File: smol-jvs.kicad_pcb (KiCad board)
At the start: 2 copper layers, 68 x 55 mm, 15 parts, among them J1 USB_B, J2 Misc, J3 Dips, J5 Power, J6 Controls, Q1 AO3400A, U1 ISL3175EIBZ-T, U2 Pico

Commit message: new gerbers and minor updates
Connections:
- U2 pad 20: /dip3 -> unconnected-(U2-Pad20)
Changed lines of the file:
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@@
   (net 41 "unconnected-(H3-Pad1)")
   (net 42 "unconnected-(H4-Pad1)")
+  (net 43 "unconnected-(U2-Pad20)")
   (footprint "Resistor_SMD:R_0805_2012Metric" (layer "F.Cu")
     (at 190.8 66.65 180)
@@
       (net 33 "/b_service") (pinfunction "GPIO14") (pintype "bidirectional"))
     (pad "20" thru_hole oval locked (at -8.89 24.13) (size 1.7 1.7) (drill 1.02) (layers *.Cu *.Mask)
-      (net 37 "/dip3") (pinfunction "GPIO15") (pintype "bidirectional"))
+      (net 43 "unconnected-(U2-Pad20)") (pinfunction "GPIO15") (pintype "bidirectional+no_connect"))
     (pad "20" smd rect locked (at -8.89 24.13) (size 3.5 1.7) (drill (offset -0.9 0)) (layers "F.Cu" "F.Mask")
-      (net 37 "/dip3") (pinfunction "GPIO15") (pintype "bidirectional"))
+      (net 43 "unconnected-(U2-Pad20)") (pinfunction "GPIO15") (pintype "bidirectional+no_connect"))
     (pad "21" smd rect locked (at 8.89 24.13) (size 3.5 1.7) (drill (offset 0.9 0)) (layers "F.Cu" "F.Mask")
       (net 12 "unconnected-(U2-Pad21)") (pinfunction "GPIO16") (pintype "bidirectional+no_connect"))
@@
     (fp_line (start -0.625 -2.35) (end 0 -1.35) (layer "F.Fab") (width 0.1))
     (pad "" np_thru_hole circle locked (at -1.6 2 270) (size 1.2 1.2) (drill 1.2) (layers *.Cu *.Mask))
-    (pad "1" thru_hole roundrect locked (at 0 0 270) (size 1.7 2) (drill 1) (layers *.Cu *.Mask) (roundrect_rratio 0.147059)
+    (pad "1" thru_hole roundrect locked (at 0 0 270) (size 1.7 2) (drill 1) (layers *.Cu *.Mask) (roundrect_rratio 0.1470588235)
       (net 34 "+5V") (pinfunction "Pin_1") (pintype "passive"))
     (pad "2" thru_hole oval locked (at 2.5 0 270) (size 1.7 2) (drill 1) (layers *.Cu *.Mask)
@@
     (fp_line (start -1.95 -1.7) (end -1.95 2.8) (layer "F.Fab") (width 0.1))
     (fp_line (start 7.95 -1.7) (end -1.95 -1.7) (layer "F.Fab") (width 0.1))
-    (pad "1" thru_hole roundrect locked (at 0 0 270) (size 1.2 1.75) (drill 0.75) (layers *.Cu *.Mask) (roundrect_rratio 0.208333)
+    (pad "1" thru_hole roundrect locked (at 0 0 270) (size 1.2 1.75) (drill 0.75) (layers *.Cu *.Mask) (roundrect_rratio 0.2083333333)
       (net 35 "/dip1") (pinfunction "Pin_1") (pintype "passive"))
     (pad "2" thru_hole oval locked (at 2 0 270) (size 1.2 1.75) (drill 0.75) (layers *.Cu *.Mask)
@@
     (fp_line (start 7.95 2.8) (end 7.95 -1.7) (layer "F.Fab") (width 0.1))
     (fp_line (start -1.11 -2.11) (end -2.36 -2.11) (layer "F.Fab") (width 0.1))
-    (pad "1" thru_hole roundrect locked (at 0 0 270) (size 1.2 1.75) (drill 0.75) (layers *.Cu *.Mask) (roundrect_rratio 0.208333)
+    (pad "1" thru_hole roundrect locked (at 0 0 270) (size 1.2 1.75) (drill 0.75) (layers *.Cu *.Mask) (roundrect_rratio 0.2083333333)
       (net 24 "/b_coin") (pinfunction "Pin_1") (pintype "passive"))
     (pad "2" thru_hole oval locked (at 2 0 270) (size 1.2 1.75) (drill 0.75) (layers *.Cu *.Mask)

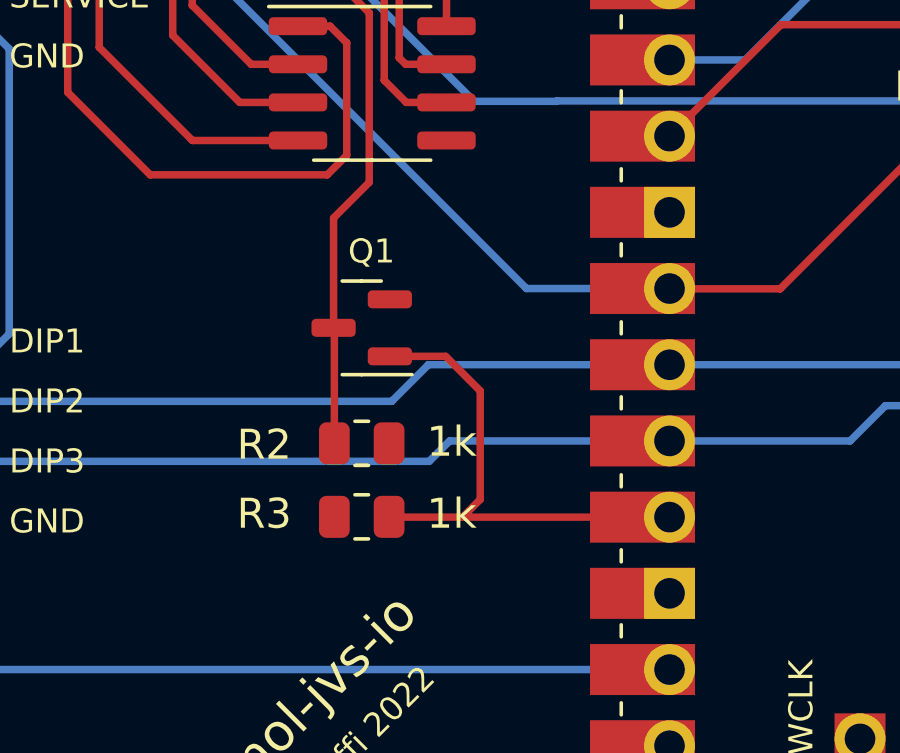
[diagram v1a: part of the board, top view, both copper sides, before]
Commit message: Go back to using diodes for sense again
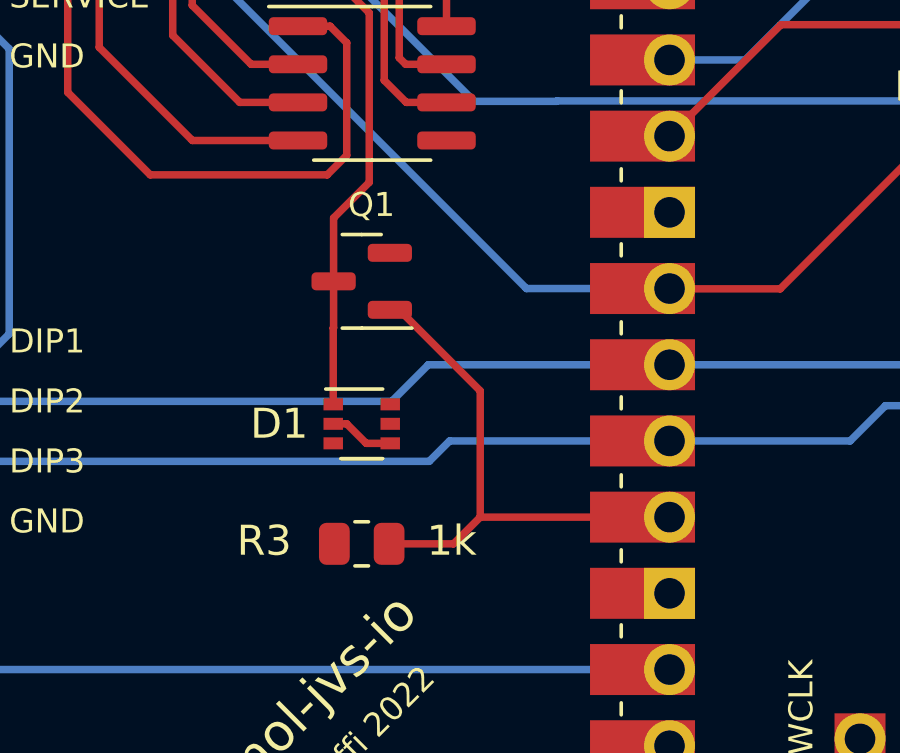
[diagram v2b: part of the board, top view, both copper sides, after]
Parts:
- removed R2: 1k, Resistor_SMD:R_0805_2012Metric
- added D1: BAV99S, Package_TO_SOT_SMD:SOT-363_SC-70-6, F.Cu at (190.8, 84.0)
- moved Q1 1.55 mm to (190.8, 79.2)
- moved R3 0.90 mm to (190.8, 88.0)
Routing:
- net Net-(D1-Pad2): track 0.00 -> 2.17 mm
- net /jvs_sense: track 26.8 -> 25.5 mm
- net /sense_0v: track 17.3 -> 18.1 mm
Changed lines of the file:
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@@
   (net 42 "unconnected-(H4-Pad1)")
   (net 43 "unconnected-(U2-Pad20)")
+  (net 44 "unconnected-(D1-Pad3)")
+  (net 45 "Net-(D1-Pad2)")
+  (net 46 "unconnected-(D1-Pad6)")
   (footprint "Resistor_SMD:R_0805_2012Metric" (layer "F.Cu")
     (at 190.8 66.65 180)
@@
   )
   (footprint "Resistor_SMD:R_0805_2012Metric" (layer "F.Cu")
-    (at 190.75 87.1 180)
+    (at 190.75 88 180)
     (descr "Resistor SMD 0805 (2012 Metric), square (rectangular) end terminal, IPC_7351 nominal, (Body size source: IPC-SM-782 page 72, https://www.pcb-3d.com/wordpress/wp-content/uploads/ipc-sm-782a_amendment_1_and_2.pdf), generated with kicad-footprint-generator")
     (tags "resistor")
@@
       (net 8 "/sense_0v") (pintype "passive"))
     (pad "2" smd roundrect (at 0.9125 0 180) (size 1.025 1.4) (layers "F.Cu" "F.Paste" "F.Mask") (roundrect_rratio 0.243902439)
-      (net 1 "GND") (pintype "passive"))
-    (model "${KICAD6_3DMODEL_DIR}/Resistor_SMD.3dshapes/R_0805_2012Metric.wrl"
-      (offset (xyz 0 0 0))
-      (scale (xyz 1 1 1))
-      (rotate (xyz 0 0 0))
-    )
-  )
-  (footprint "Resistor_SMD:R_0805_2012Metric" (layer "F.Cu")
-    (at 190.75 84.65)
-    (descr "Resistor SMD 0805 (2012 Metric), square (rectangular) end terminal, IPC_7351 nominal, (Body size source: IPC-SM-782 page 72, https://www.pcb-3d.com/wordpress/wp-content/uploads/ipc-sm-782a_amendment_1_and_2.pdf), generated with kicad-footprint-generator")
-    (tags "resistor")
-    (property "Digikey" "311-100CRCT-ND")
-    (property "Sheetfile" "smol-jvs.kicad_sch")
-    (property "Sheetname" "")
-    (attr smd)
-    (fp_text reference "R2" (at -3.25 0.05) (layer "F.SilkS")
-      (effects (font (size 1 1) (thickness 0.15)))
-    )
-    (fp_text value "1k" (at 3 -0.05) (layer "F.SilkS")
-      (effects (font (size 1 1) (thickness 0.15)))
-    )
-    (fp_text user "${REFERENCE}" (at 0 0) (layer "F.Fab")
-      (effects (font (size 0.5 0.5) (thickness 0.08)))
-    )
-    (fp_line (start -0.227064 0.735) (end 0.227064 0.735) (layer "F.SilkS") (width 0.12))
-    (fp_line (start -0.227064 -0.735) (end 0.227064 -0.735) (layer "F.SilkS") (width 0.12))
-    (fp_line (start 1.68 -0.95) (end 1.68 0.95) (layer "F.CrtYd") (width 0.05))
-    (fp_line (start -1.68 -0.95) (end 1.68 -0.95) (layer "F.CrtYd") (width 0.05))
-    (fp_line (start 1.68 0.95) (end -1.68 0.95) (layer "F.CrtYd") (width 0.05))
-    (fp_line (start -1.68 0.95) (end -1.68 -0.95) (layer "F.CrtYd") (width 0.05))
-    (fp_line (start -1 0.625) (end -1 -0.625) (layer "F.Fab") (width 0.1))
-    (fp_line (start 1 0.625) (end -1 0.625) (layer "F.Fab") (width 0.1))
-    (fp_line (start -1 -0.625) (end 1 -0.625) (layer "F.Fab") (width 0.1))
-    (fp_line (start 1 -0.625) (end 1 0.625) (layer "F.Fab") (width 0.1))
-    (pad "1" smd roundrect (at -0.9125 0) (size 1.025 1.4) (layers "F.Cu" "F.Paste" "F.Mask") (roundrect_rratio 0.243902439)
-      (net 39 "/jvs_sense") (pintype "passive"))
-    (pad "2" smd roundrect (at 0.9125 0) (size 1.025 1.4) (layers "F.Cu" "F.Paste" "F.Mask") (roundrect_rratio 0.243902439)
       (net 1 "GND") (pintype "passive"))
     (model "${KICAD6_3DMODEL_DIR}/Resistor_SMD.3dshapes/R_0805_2012Metric.wrl"
@@
       (net 38 "unconnected-(U2-Pad43)") (pinfunction "SWDIO") (pintype "bidirectional+no_connect"))
   )
+  (footprint "Package_TO_SOT_SMD:SOT-363_SC-70-6" (layer "F.Cu")
+    (at 190.75 84)
+    (descr "SOT-363, SC-70-6")
+    (tags "SOT-363 SC-70-6")
+    (property "Sheetfile" "smol-jvs.kicad_sch")
+    (property "Sheetname" "")
+    (attr smd)
+    (fp_text reference "D1" (at -2.75 0) (layer "F.SilkS")
+      (effects (font (size 1 1) (thickness 0.15)))
+    )
+    (fp_text value "BAV99S" (at 0 2 180) (layer "F.Fab")
+      (effects (font (size 1 1) (thickness 0.15)))
+    )
+    (fp_text user "${REFERENCE}" (at 0 0 90) (layer "F.Fab")
+      (effects (font (size 0.5 0.5) (thickness 0.075)))
+    )
+    (fp_line (start 0.7 -1.16) (end -1.2 -1.16) (layer "F.SilkS") (width 0.12))
+    (fp_line (start -0.7 1.16) (end 0.7 1.16) (layer "F.SilkS") (width 0.12))
+    (fp_line (start 1.6 1.4) (end 1.6 -1.4) (layer "F.CrtYd") (width 0.05))
+    (fp_line (start -1.6 -1.4) (end -1.6 1.4) (layer "F.CrtYd") (width 0.05))
+    (fp_line (start -1.6 -1.4) (end 1.6 -1.4) (layer "F.CrtYd") (width 0.05))
+    (fp_line (start -1.6 1.4) (end 1.6 1.4) (layer "F.CrtYd") (width 0.05))
+    (fp_line (start 0.675 1.1) (end -0.675 1.1) (layer "F.Fab") (width 0.1))
+    (fp_line (start 0.675 -1.1) (end 0.675 1.1) (layer "F.Fab") (width 0.1))
+    (fp_line (start -0.175 -1.1) (end -0.675 -0.6) (layer "F.Fab") (width 0.1))
+    (fp_line (start 0.675 -1.1) (end -0.175 -1.1) (layer "F.Fab") (width 0.1))
+    (fp_line (start -0.675 -0.6) (end -0.675 1.1) (layer "F.Fab") (width 0.1))
+    (pad "1" smd rect locked (at -0.95 -0.65) (size 0.65 0.4) (layers "F.Cu" "F.Paste" "F.Mask")
+      (net 39 "/jvs_sense") (pinfunction "A1") (pintype "passive"))
+    (pad "2" smd rect locked (at -0.95 0) (size 0.65 0.4) (layers "F.Cu" "F.Paste" "F.Mask")
+      (net 45 "Net-(D1-Pad2)") (pinfunction "K2") (pintype "passive"))
+    (pad "3" smd rect locked (at -0.95 0.65) (size 0.65 0.4) (layers "F.Cu" "F.Paste" "F.Mask")
+      (net 44 "unconnected-(D1-Pad3)") (pinfunction "K1A2") (pintype "passive+no_connect"))
+    (pad "4" smd rect locked (at 0.95 0.65) (size 0.65 0.4) (layers "F.Cu" "F.Paste" "F.Mask")
+      (net 45 "Net-(D1-Pad2)") (pinfunction "A3") (pintype "passive"))
+    (pad "5" smd rect locked (at 0.95 0) (size 0.65 0.4) (layers "F.Cu" "F.Paste" "F.Mask")
+      (net 1 "GND") (pinfunction "K4") (pintype "passive"))
+    (pad "6" smd rect locked (at 0.95 -0.65) (size 0.65 0.4) (layers "F.Cu" "F.Paste" "F.Mask")
+      (net 46 "unconnected-(D1-Pad6)") (pinfunction "K3A4") (pintype "passive+no_connect"))
+    (model "${KICAD6_3DMODEL_DIR}/Package_TO_SOT_SMD.3dshapes/SOT-363_SC-70-6.wrl"
+      (offset (xyz 0 0 0))
+      (scale (xyz 1 1 1))
+      (rotate (xyz 0 0 0))
+    )
+  )
   (footprint "Connector_JST:JST_XH_B2B-XH-AM_1x02_P2.50mm_Vertical" (layer "F.Cu")
     (at 235 55 -90)
@@
   )
   (footprint "Package_TO_SOT_SMD:SOT-23" (layer "F.Cu")
-    (at 190.75 80.8 180)
+    (at 190.75 79.25 180)
     (descr "SOT, 3 Pin (https://www.jedec.org/system/files/docs/to-236h.pdf variant AB), generated with kicad-footprint-generator ipc_gullwing_generator.py")
     (tags "SOT TO_SOT_SMD")
@@
   (segment (start 189.6 75.7) (end 183.7 75.7) (width 0.25) (layer "F.Cu") (net 7))
   (segment (start 182.59 49.01) (end 201.01 49.01) (width 0.25) (layer "F.Cu") (net 7))
-  (segment (start 191.6875 81.75) (end 193.55 81.75) (width 0.25) (layer "F.Cu") (net 8))
-  (segment (start 191.6725 87.11) (end 194.11 87.11) (width 0.25) (layer "F.Cu") (net 8))
-  (segment (start 194.7 86.52) (end 194.11 87.11) (width 0.25) (layer "F.Cu") (net 8))
-  (segment (start 194.11 87.11) (end 201.01 87.11) (width 0.25) (layer "F.Cu") (net 8))
-  (segment (start 193.55 81.75) (end 194.7 82.9) (width 0.25) (layer "F.Cu") (net 8))
-  (segment (start 194.7 82.9) (end 194.7 86.52) (width 0.25) (layer "F.Cu") (net 8))
-  (segment (start 191.6625 87.1) (end 191.6725 87.11) (width 0.25) (layer "F.Cu") (net 8))
+  (segment (start 191.6875 80.2) (end 192 80.2) (width 0.25) (layer "F.Cu") (net 8))
+  (segment (start 192 80.2) (end 194.7 82.9) (width 0.25) (layer "F.Cu") (net 8))
+  (segment (start 194.7 82.9) (end 194.7 87.11) (width 0.25) (layer "F.Cu") (net 8))
+  (segment (start 191.6625 88) (end 193.81 88) (width 0.25) (layer "F.Cu") (net 8))
+  (segment (start 193.81 88) (end 194.7 87.11) (width 0.25) (layer "F.Cu") (net 8))
+  (segment (start 194.7 87.11) (end 201.01 87.11) (width 0.25) (layer "F.Cu") (net 8))
   (segment (start 192.215 72.015) (end 193.575 72.015) (width 0.25) (layer "F.Cu") (net 10))
   (segment (start 192 69.05) (end 192 71.8) (width 0.25) (layer "F.Cu") (net 10))
@@
   (segment (start 193 85.25) (end 193.68 84.57) (width 0.25) (layer "B.Cu") (net 37))
   (segment (start 176.3 85.25) (end 193 85.25) (width 0.25) (layer "B.Cu") (net 37))
+  (segment (start 186.8 66.1) (end 186.8 64.35) (width 0.25) (layer "F.Cu") (net 39))
   (segment (start 191 70.3) (end 186.8 66.1) (width 0.25) (layer "F.Cu") (net 39))
+  (segment (start 186.75 64.3) (end 186.75 60.0775) (width 0.25) (layer "F.Cu") (net 39))
+  (segment (start 189.8125 80.8) (end 189.8 80.8125) (width 0.25) (layer "F.Cu") (net 39))
+  (segment (start 189.8125 77.1375) (end 191 75.95) (width 0.25) (layer "F.Cu") (net 39))
   (segment (start 186.8 64.35) (end 186.75 64.3) (width 0.25) (layer "F.Cu") (net 39))
+  (segment (start 189.8125 80.8) (end 189.8125 77.1375) (width 0.25) (layer "F.Cu") (net 39))
   (segment (start 191 75.95) (end 191 70.3) (width 0.25) (layer "F.Cu") (net 39))
-  (segment (start 186.75 64.3) (end 186.75 60.0775) (width 0.25) (layer "F.Cu") (net 39))
-  (segment (start 186.8 66.1) (end 186.8 64.35) (width 0.25) (layer "F.Cu") (net 39))
-  (segment (start 189.8375 80.825) (end 189.8125 80.8) (width 0.25) (layer "F.Cu") (net 39))
-  (segment (start 189.8125 80.8) (end 189.8125 77.1375) (width 0.25) (layer "F.Cu") (net 39))
-  (segment (start 189.8375 84.65) (end 189.8375 80.825) (width 0.25) (layer "F.Cu") (net 39))
-  (segment (start 189.8125 77.1375) (end 191 75.95) (width 0.25) (layer "F.Cu") (net 39))
+  (segment (start 189.8 80.8125) (end 189.8 83.35) (width 0.25) (layer "F.Cu") (net 39))
+  (segment (start 190.25 84) (end 189.8 84) (width 0.25) (layer "F.Cu") (net 45))
+  (segment (start 190.9 84.65) (end 190.25 84) (width 0.25) (layer "F.Cu") (net 45))
+  (segment (start 191.7 84.65) (end 190.9 84.65) (width 0.25) (layer "F.Cu") (net 45))
   (zone (net 1) (net_name "GND") (layers F&B.Cu) (hatch edge 0.508)
     (connect_pads (clearance 0.1))
